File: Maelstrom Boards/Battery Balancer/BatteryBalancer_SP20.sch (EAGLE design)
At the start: 83 parts, among them IC3 REG1117, P1 39-30-14, P2 39-30-16, Q1 SPB80P06P, Q10 MOSFET-NCH-AO3404A, Q11 MOSFET-NCH-AO3404A, Q19 FDD4141TO252, Q2 SPB80P06P, Q22 FDD4141TO252, Q3 NMOSFET-D2PAK-7, Q4 310mA/60V/1.6Ω, Q5 NMOSFET-D2PAK-7, Q6 FDD4141TO252, Q7 MOSFET-NCH-AO3404A, Q8 MOSFET-NCH-AO3404A, Q9 MOSFET-NCH-AO3404A

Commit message: Changed Top Connector Position
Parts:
- removed P1: 39-30-14, con-molex-mini-fit:39-30-14
- added U$4: 14PIN-VERT, Vertical_Connectors:14PIN-VERT
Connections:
- net GND: now also U$4.1-, U$4.2-, U$4.3-, U$4.4-, U$4.5-, U$4.6-, U$4.7-; no longer P1.10, P1.11, P1.12, P1.13, P1.14, P1.8, P1.9
- net MOTOR_POWER: now also U$4.1+, U$4.2+, U$4.3+, U$4.4+, U$4.5+, U$4.6+, U$4.7+; no longer P1.1, P1.2, P1.3, P1.4, P1.5, P1.6, P1.7
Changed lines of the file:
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@@
 <part name="+3V1" library="supply1" library_urn="urn:adsk.eagle:library:371" deviceset="+3V3" device=""/>
 <part name="FRAME1" library="frames" library_urn="urn:adsk.eagle:library:229" deviceset="A3L-LOC" device="" value="a"/>
-<part name="GND4" library="supply1" library_urn="urn:adsk.eagle:library:371" deviceset="GND" device=""/>
 <part name="GND16" library="supply1" library_urn="urn:adsk.eagle:library:371" deviceset="GND" device=""/>
 <part name="P2" library="con-molex-mini-fit" deviceset="39-30-?16?" device=""/>
@@
 <part name="+3V9" library="supply1" library_urn="urn:adsk.eagle:library:371" deviceset="+3V3" device=""/>
 <part name="GND3" library="supply1" library_urn="urn:adsk.eagle:library:371" deviceset="GND" device=""/>
-<part name="P1" library="con-molex-mini-fit" deviceset="39-30-?14?" device=""/>
 <part name="GND15" library="supply1" library_urn="urn:adsk.eagle:library:371" deviceset="GND" device=""/>
 <part name="GND24" library="supply1" library_urn="urn:adsk.eagle:library:371" deviceset="GND" device=""/>
 <part name="GND25" library="supply1" library_urn="urn:adsk.eagle:library:371" deviceset="GND" device=""/>
+<part name="GND4" library="supply1" library_urn="urn:adsk.eagle:library:371" deviceset="GND" device=""/>
+<part name="U$4" library="Vertical_Connectors" deviceset="14PIN-VERT" device=""/>
 </parts>
 <sheets>
@@
 <attribute name="SHEET" x="357.680259375" y="4.9784" size="2.54" layer="94"/>
 </instance>
-<instance part="GND4" gate="1" x="353.06" y="96.52" smashed="yes">
-<attribute name="VALUE" x="350.52" y="93.98" size="1.778" layer="96"/>
-</instance>
 <instance part="GND16" gate="1" x="208.28" y="170.18" smashed="yes">
 <attribute name="VALUE" x="205.74" y="167.64" size="1.778" layer="96"/>
@@
 <attribute name="VALUE" x="88.9" y="182.88" size="1.778" layer="96"/>
 </instance>
-<instance part="P1" gate="G$1" x="335.28" y="101.6" smashed="yes">
-<attribute name="NAME" x="331.47" y="112.395" size="1.778" layer="95"/>
-<attribute name="VALUE" x="331.47" y="88.9" size="1.778" layer="95"/>
+<instance part="GND4" gate="1" x="327.66" y="104.14" smashed="yes">
+<attribute name="VALUE" x="325.12" y="101.6" size="1.778" layer="96"/>
 </instance>
+<instance part="U$4" gate="G$1" x="297.18" y="91.44" smashed="yes"/>
 </instances>
 <busses>
@@
 </segment>
 <segment>
+<pinref part="U$4" gate="G$1" pin="7-"/>
+<wire x1="312.42" y1="124.46" x2="320.04" y2="124.46" width="0.1524" layer="91"/>
+<wire x1="320.04" y1="124.46" x2="320.04" y2="119.38" width="0.1524" layer="91"/>
+<pinref part="U$4" gate="G$1" pin="1-"/>
+<wire x1="320.04" y1="119.38" x2="320.04" y2="114.3" width="0.1524" layer="91"/>
+<wire x1="320.04" y1="114.3" x2="320.04" y2="109.22" width="0.1524" layer="91"/>
+<wire x1="320.04" y1="109.22" x2="320.04" y2="104.14" width="0.1524" layer="91"/>
+<wire x1="320.04" y1="104.14" x2="320.04" y2="99.06" width="0.1524" layer="91"/>
+<wire x1="320.04" y1="99.06" x2="320.04" y2="93.98" width="0.1524" layer="91"/>
+<wire x1="320.04" y1="93.98" x2="312.42" y2="93.98" width="0.1524" layer="91"/>
+<pinref part="U$4" gate="G$1" pin="2-"/>
+<wire x1="312.42" y1="99.06" x2="320.04" y2="99.06" width="0.1524" layer="91"/>
+<junction x="320.04" y="99.06"/>
+<pinref part="U$4" gate="G$1" pin="3-"/>
+<wire x1="312.42" y1="104.14" x2="320.04" y2="104.14" width="0.1524" layer="91"/>
+<junction x="320.04" y="104.14"/>
+<pinref part="U$4" gate="G$1" pin="4-"/>
+<wire x1="312.42" y1="109.22" x2="320.04" y2="109.22" width="0.1524" layer="91"/>
+<junction x="320.04" y="109.22"/>
+<pinref part="U$4" gate="G$1" pin="5-"/>
+<wire x1="312.42" y1="114.3" x2="320.04" y2="114.3" width="0.1524" layer="91"/>
+<junction x="320.04" y="114.3"/>
+<pinref part="U$4" gate="G$1" pin="6-"/>
+<wire x1="312.42" y1="119.38" x2="320.04" y2="119.38" width="0.1524" layer="91"/>
+<junction x="320.04" y="119.38"/>
+<wire x1="320.04" y1="109.22" x2="327.66" y2="109.22" width="0.1524" layer="91"/>
 <pinref part="GND4" gate="1" pin="GND"/>
-<wire x1="353.06" y1="101.6" x2="353.06" y2="99.06" width="0.1524" layer="91"/>
-<pinref part="P1" gate="G$1" pin="10"/>
-<wire x1="342.9" y1="99.06" x2="345.44" y2="99.06" width="0.1524" layer="91"/>
-<wire x1="345.44" y1="99.06" x2="345.44" y2="101.6" width="0.1524" layer="91"/>
-<pinref part="P1" gate="G$1" pin="8"/>
-<wire x1="342.9" y1="101.6" x2="345.44" y2="101.6" width="0.1524" layer="91"/>
-<junction x="345.44" y="101.6"/>
-<pinref part="P1" gate="G$1" pin="12"/>
-<wire x1="342.9" y1="96.52" x2="345.44" y2="96.52" width="0.1524" layer="91"/>
-<wire x1="345.44" y1="96.52" x2="345.44" y2="99.06" width="0.1524" layer="91"/>
-<junction x="345.44" y="99.06"/>
-<pinref part="P1" gate="G$1" pin="14"/>
-<wire x1="342.9" y1="93.98" x2="345.44" y2="93.98" width="0.1524" layer="91"/>
-<wire x1="345.44" y1="93.98" x2="345.44" y2="96.52" width="0.1524" layer="91"/>
-<junction x="345.44" y="96.52"/>
-<wire x1="353.06" y1="101.6" x2="345.44" y2="101.6" width="0.1524" layer="91"/>
-<pinref part="P1" gate="G$1" pin="13"/>
-<pinref part="P1" gate="G$1" pin="11"/>
-<pinref part="P1" gate="G$1" pin="9"/>
-<wire x1="327.66" y1="99.06" x2="325.12" y2="99.06" width="0.1524" layer="91"/>
-<wire x1="325.12" y1="99.06" x2="325.12" y2="96.52" width="0.1524" layer="91"/>
-<wire x1="325.12" y1="96.52" x2="327.66" y2="96.52" width="0.1524" layer="91"/>
-<junction x="325.12" y="96.52"/>
-<wire x1="325.12" y1="96.52" x2="325.12" y2="93.98" width="0.1524" layer="91"/>
-<wire x1="325.12" y1="93.98" x2="327.66" y2="93.98" width="0.1524" layer="91"/>
-<wire x1="325.12" y1="93.98" x2="325.12" y2="86.36" width="0.1524" layer="91"/>
-<junction x="325.12" y="93.98"/>
-<wire x1="325.12" y1="86.36" x2="345.44" y2="86.36" width="0.1524" layer="91"/>
-<wire x1="345.44" y1="86.36" x2="345.44" y2="93.98" width="0.1524" layer="91"/>
-<junction x="345.44" y="93.98"/>
+<wire x1="327.66" y1="109.22" x2="327.66" y2="106.68" width="0.1524" layer="91"/>
 </segment>
 </net>
@@
 <junction x="198.12" y="228.6"/>
 <label x="205.74" y="233.68" size="1.778" layer="95" xref="yes"/>
-</segment>
-</net>
-<net name="MOTOR_POWER" class="0">
-<segment>
-<wire x1="325.12" y1="101.6" x2="312.42" y2="101.6" width="0.1524" layer="91"/>
-<label x="312.42" y="101.6" size="1.778" layer="95" rot="R180" xref="yes"/>
-<pinref part="P1" gate="G$1" pin="1"/>
-<wire x1="327.66" y1="109.22" x2="325.12" y2="109.22" width="0.1524" layer="91"/>
-<wire x1="325.12" y1="109.22" x2="325.12" y2="106.68" width="0.1524" layer="91"/>
-<pinref part="P1" gate="G$1" pin="3"/>
-<wire x1="325.12" y1="106.68" x2="327.66" y2="106.68" width="0.1524" layer="91"/>
-<wire x1="325.12" y1="106.68" x2="325.12" y2="104.14" width="0.1524" layer="91"/>
-<junction x="325.12" y="106.68"/>
-<pinref part="P1" gate="G$1" pin="5"/>
-<wire x1="325.12" y1="104.14" x2="327.66" y2="104.14" width="0.1524" layer="91"/>
-<wire x1="325.12" y1="104.14" x2="325.12" y2="101.6" width="0.1524" layer="91"/>
-<junction x="325.12" y="104.14"/>
-<pinref part="P1" gate="G$1" pin="7"/>
-<wire x1="325.12" y1="101.6" x2="327.66" y2="101.6" width="0.1524" layer="91"/>
-<junction x="325.12" y="101.6"/>
-<wire x1="325.12" y1="109.22" x2="325.12" y2="116.84" width="0.1524" layer="91"/>
-<junction x="325.12" y="109.22"/>
-<wire x1="325.12" y1="116.84" x2="345.44" y2="116.84" width="0.1524" layer="91"/>
-<pinref part="P1" gate="G$1" pin="2"/>
-<wire x1="345.44" y1="109.22" x2="342.9" y2="109.22" width="0.1524" layer="91"/>
-<pinref part="P1" gate="G$1" pin="4"/>
-<wire x1="342.9" y1="106.68" x2="345.44" y2="106.68" width="0.1524" layer="91"/>
-<junction x="345.44" y="106.68"/>
-<wire x1="345.44" y1="106.68" x2="345.44" y2="109.22" width="0.1524" layer="91"/>
-<wire x1="345.44" y1="104.14" x2="345.44" y2="106.68" width="0.1524" layer="91"/>
-<pinref part="P1" gate="G$1" pin="6"/>
-<wire x1="342.9" y1="104.14" x2="345.44" y2="104.14" width="0.1524" layer="91"/>
-<wire x1="345.44" y1="116.84" x2="345.44" y2="109.22" width="0.1524" layer="91"/>
-<junction x="345.44" y="109.22"/>
 </segment>
 </net>
@@
 </segment>
 </net>
+<net name="MOTOR_POWER" class="0">
+<segment>
+<pinref part="U$4" gate="G$1" pin="7+"/>
+<wire x1="292.1" y1="124.46" x2="284.48" y2="124.46" width="0.1524" layer="91"/>
+<pinref part="U$4" gate="G$1" pin="1+"/>
+<wire x1="284.48" y1="124.46" x2="284.48" y2="119.38" width="0.1524" layer="91"/>
+<wire x1="284.48" y1="119.38" x2="284.48" y2="114.3" width="0.1524" layer="91"/>
+<wire x1="284.48" y1="114.3" x2="284.48" y2="109.22" width="0.1524" layer="91"/>
+<wire x1="284.48" y1="109.22" x2="284.48" y2="104.14" width="0.1524" layer="91"/>
+<wire x1="284.48" y1="104.14" x2="284.48" y2="99.06" width="0.1524" layer="91"/>
+<wire x1="284.48" y1="99.06" x2="284.48" y2="93.98" width="0.1524" layer="91"/>
+<wire x1="284.48" y1="93.98" x2="292.1" y2="93.98" width="0.1524" layer="91"/>
+<pinref part="U$4" gate="G$1" pin="2+"/>
+<wire x1="292.1" y1="99.06" x2="284.48" y2="99.06" width="0.1524" layer="91"/>
+<junction x="284.48" y="99.06"/>
+<pinref part="U$4" gate="G$1" pin="3+"/>
+<wire x1="292.1" y1="104.14" x2="284.48" y2="104.14" width="0.1524" layer="91"/>
+<junction x="284.48" y="104.14"/>
+<pinref part="U$4" gate="G$1" pin="4+"/>
+<wire x1="292.1" y1="109.22" x2="284.48" y2="109.22" width="0.1524" layer="91"/>
+<junction x="284.48" y="109.22"/>
+<pinref part="U$4" gate="G$1" pin="5+"/>
+<wire x1="292.1" y1="114.3" x2="284.48" y2="114.3" width="0.1524" layer="91"/>
+<junction x="284.48" y="114.3"/>
+<pinref part="U$4" gate="G$1" pin="6+"/>
+<wire x1="292.1" y1="119.38" x2="284.48" y2="119.38" width="0.1524" layer="91"/>
+<junction x="284.48" y="119.38"/>
+<wire x1="284.48" y1="109.22" x2="274.32" y2="109.22" width="0.1524" layer="91"/>
+<label x="274.32" y="109.22" size="1.778" layer="95" rot="R180" xref="yes"/>
+</segment>
+</net>

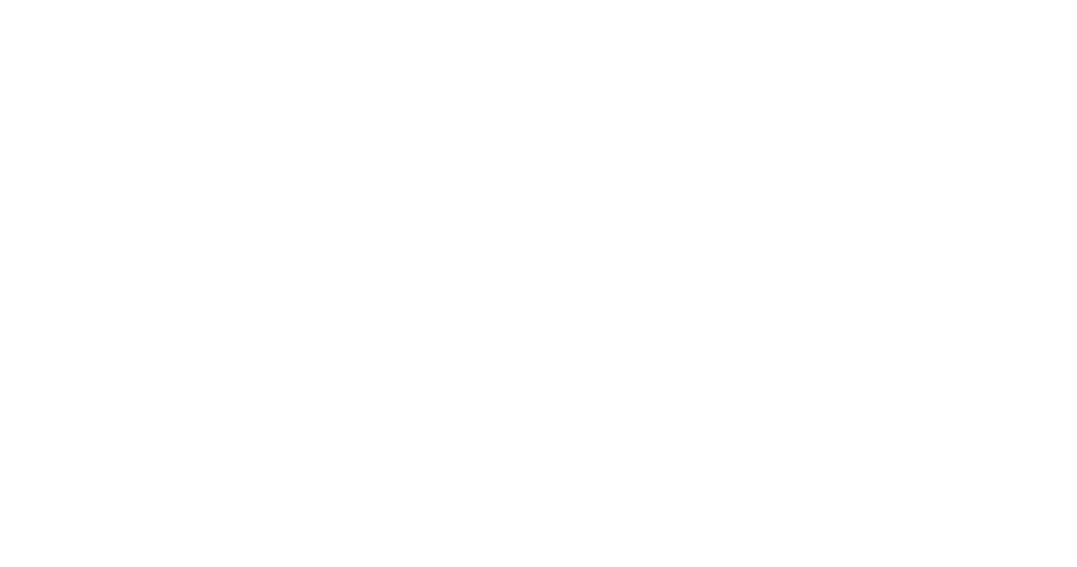
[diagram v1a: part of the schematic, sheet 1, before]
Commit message: Added connector to BB
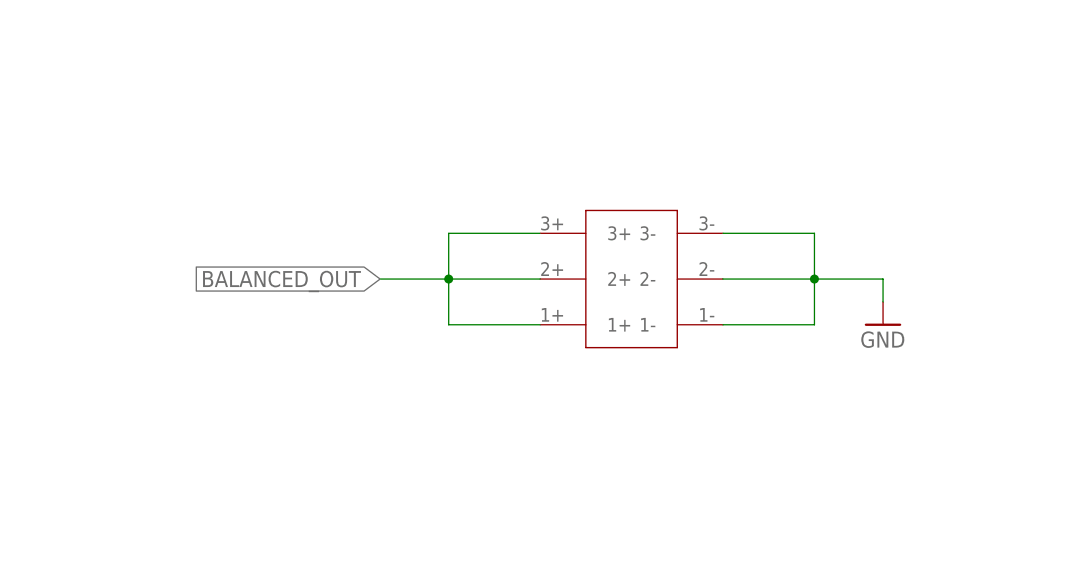
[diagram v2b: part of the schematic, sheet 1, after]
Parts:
- added U$13: 6PIN-VERT, Vertical_Connectors:6PIN-VERT
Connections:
- removed net V+: L1.1, L3.1, R20.1, R22.1, R5.1
- net BALANCED_OUT: now also L1.1, L3.1, R20.1, R22.1, R5.1, U$13.1+, U$13.2+, U$13.3+
- net GND: now also U$13.1-, U$13.2-, U$13.3-
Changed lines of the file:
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@@
 <part name="P+2" library="supply1" library_urn="urn:adsk.eagle:library:371" deviceset="+12V" device=""/>
 <part name="Q11" library="SparkFun-DiscreteSemi" deviceset="MOSFET-NCH" device="-AO3404A" value=""/>
-<part name="P+3" library="supply1" library_urn="urn:adsk.eagle:library:371" deviceset="V+" device=""/>
+<part name="BALANCED_OUT" library="supply1" library_urn="urn:adsk.eagle:library:371" deviceset="V+" device=""/>
 <part name="P+4" library="supply1" library_urn="urn:adsk.eagle:library:371" deviceset="V+" device=""/>
 <part name="P+8" library="supply1" library_urn="urn:adsk.eagle:library:371" deviceset="V+" device=""/>
@@
 <part name="GND4" library="supply1" library_urn="urn:adsk.eagle:library:371" deviceset="GND" device=""/>
 <part name="U$4" library="Vertical_Connectors" deviceset="14PIN-VERT" device=""/>
+<part name="U$13" library="Vertical_Connectors" deviceset="6PIN-VERT" device=""/>
+<part name="GND26" library="supply1" library_urn="urn:adsk.eagle:library:371" deviceset="GND" device=""/>
 </parts>
 <sheets>
@@
 </instance>
 <instance part="U$4" gate="G$1" x="297.18" y="91.44" smashed="yes"/>
+<instance part="U$13" gate="G$1" x="307.34" y="187.96" smashed="yes"/>
+<instance part="GND26" gate="1" x="340.36" y="190.5" smashed="yes">
+<attribute name="VALUE" x="337.82" y="187.96" size="1.778" layer="96"/>
+</instance>
 </instances>
 <busses>
@@
 <wire x1="327.66" y1="109.22" x2="327.66" y2="106.68" width="0.1524" layer="91"/>
 </segment>
+<segment>
+<pinref part="GND26" gate="1" pin="GND"/>
+<wire x1="340.36" y1="193.04" x2="340.36" y2="195.58" width="0.1524" layer="91"/>
+<wire x1="340.36" y1="195.58" x2="332.74" y2="195.58" width="0.1524" layer="91"/>
+<pinref part="U$13" gate="G$1" pin="3-"/>
+<wire x1="322.58" y1="200.66" x2="332.74" y2="200.66" width="0.1524" layer="91"/>
+<wire x1="332.74" y1="200.66" x2="332.74" y2="195.58" width="0.1524" layer="91"/>
+<pinref part="U$13" gate="G$1" pin="1-"/>
+<wire x1="332.74" y1="195.58" x2="332.74" y2="190.5" width="0.1524" layer="91"/>
+<wire x1="332.74" y1="190.5" x2="322.58" y2="190.5" width="0.1524" layer="91"/>
+<pinref part="U$13" gate="G$1" pin="2-"/>
+<wire x1="322.58" y1="195.58" x2="332.74" y2="195.58" width="0.1524" layer="91"/>
+<junction x="332.74" y="195.58"/>
+</segment>
 </net>
 <net name="STBD_BATTERY" class="0">
@@
 </segment>
 </net>
+<net name="BALANCED_OUT" class="0">
+<segment>
+<pinref part="U$13" gate="G$1" pin="1+"/>
+<wire x1="302.26" y1="190.5" x2="292.1" y2="190.5" width="0.1524" layer="91"/>
+<wire x1="292.1" y1="190.5" x2="292.1" y2="195.58" width="0.1524" layer="91"/>
+<pinref part="U$13" gate="G$1" pin="3+"/>
+<wire x1="292.1" y1="195.58" x2="292.1" y2="200.66" width="0.1524" layer="91"/>
+<wire x1="292.1" y1="200.66" x2="302.26" y2="200.66" width="0.1524" layer="91"/>
+<pinref part="U$13" gate="G$1" pin="2+"/>
+<wire x1="302.26" y1="195.58" x2="292.1" y2="195.58" width="0.1524" layer="91"/>
+<junction x="292.1" y="195.58"/>
+<wire x1="292.1" y1="195.58" x2="284.48" y2="195.58" width="0.1524" layer="91"/>
+<label x="284.48" y="195.58" size="1.778" layer="95" rot="R180" xref="yes"/>
+</segment>
+</net>
 </nets>
 </sheet>
@@
 <attribute name="VALUE" x="227.33" y="159.258" size="1.778" layer="96"/>
 </instance>
-<instance part="P+3" gate="1" x="233.68" y="200.66" smashed="yes" rot="R270">
-<attribute name="VALUE" x="231.14" y="203.2" size="1.778" layer="96"/>
-</instance>
+<instance part="BALANCED_OUT" gate="1" x="233.68" y="200.66" smashed="yes" rot="R270"/>
 </instances>
 <busses>
@@
 </segment>
 </net>
-<net name="BALANCED_OUT" class="0">
-<segment>
-<pinref part="U$2" gate="G$1" pin="OUT"/>
-<wire x1="193.04" y1="218.44" x2="193.04" y2="215.9" width="0.1524" layer="91"/>
-<wire x1="193.04" y1="218.44" x2="210.82" y2="218.44" width="0.1524" layer="91"/>
-<wire x1="210.82" y1="218.44" x2="210.82" y2="208.28" width="0.1524" layer="91"/>
-<junction x="193.04" y="218.44"/>
-<pinref part="U$2" gate="G$1" pin="VS"/>
-<wire x1="210.82" y1="208.28" x2="210.82" y2="198.12" width="0.1524" layer="91"/>
-<wire x1="210.82" y1="198.12" x2="203.2" y2="198.12" width="0.1524" layer="91"/>
-<wire x1="210.82" y1="208.28" x2="220.98" y2="208.28" width="0.1524" layer="91"/>
-<junction x="210.82" y="208.28"/>
-<wire x1="208.28" y1="109.22" x2="220.98" y2="109.22" width="0.1524" layer="91"/>
-<pinref part="U$3" gate="G$1" pin="OUT"/>
-<wire x1="193.04" y1="129.54" x2="193.04" y2="127" width="0.1524" layer="91"/>
-<junction x="193.04" y="129.54"/>
-<wire x1="193.04" y1="129.54" x2="208.28" y2="129.54" width="0.1524" layer="91"/>
-<wire x1="208.28" y1="129.54" x2="208.28" y2="109.22" width="0.1524" layer="91"/>
-<junction x="208.28" y="109.22"/>
-<pinref part="U$3" gate="G$1" pin="VS"/>
-<wire x1="203.2" y1="109.22" x2="208.28" y2="109.22" width="0.1524" layer="91"/>
-<wire x1="220.98" y1="109.22" x2="220.98" y2="162.56" width="0.1524" layer="91"/>
-<wire x1="220.98" y1="162.56" x2="220.98" y2="170.18" width="0.1524" layer="91"/>
-<wire x1="220.98" y1="170.18" x2="220.98" y2="208.28" width="0.1524" layer="91"/>
-<wire x1="226.06" y1="170.18" x2="220.98" y2="170.18" width="0.1524" layer="91"/>
-<junction x="220.98" y="170.18"/>
-<pinref part="R12" gate="G$1" pin="1"/>
-<pinref part="Q3" gate="G$1" pin="D"/>
-<wire x1="190.5" y1="233.68" x2="193.04" y2="233.68" width="0.1524" layer="91"/>
-<wire x1="193.04" y1="233.68" x2="193.04" y2="218.44" width="0.1524" layer="91"/>
-<pinref part="Q5" gate="G$1" pin="D"/>
-<wire x1="190.5" y1="144.78" x2="193.04" y2="144.78" width="0.1524" layer="91"/>
-<wire x1="193.04" y1="144.78" x2="193.04" y2="129.54" width="0.1524" layer="91"/>
-<pinref part="R19" gate="G$1" pin="1"/>
-<wire x1="226.06" y1="162.56" x2="220.98" y2="162.56" width="0.1524" layer="91"/>
-<junction x="220.98" y="162.56"/>
-</segment>
-</net>
 <net name="N$11" class="0">
 <segment>
@@
 </segment>
 </net>
-<net name="V+" class="0">
+<net name="BALANCED_OUT" class="0">
 <segment>
-<pinref part="P+3" gate="1" pin="V+"/>
+<pinref part="U$2" gate="G$1" pin="OUT"/>
+<wire x1="193.04" y1="218.44" x2="193.04" y2="215.9" width="0.1524" layer="91"/>
+<wire x1="193.04" y1="218.44" x2="210.82" y2="218.44" width="0.1524" layer="91"/>
+<wire x1="210.82" y1="218.44" x2="210.82" y2="208.28" width="0.1524" layer="91"/>
+<junction x="193.04" y="218.44"/>
+<pinref part="U$2" gate="G$1" pin="VS"/>
+<wire x1="210.82" y1="208.28" x2="210.82" y2="198.12" width="0.1524" layer="91"/>
+<wire x1="210.82" y1="198.12" x2="203.2" y2="198.12" width="0.1524" layer="91"/>
+<wire x1="210.82" y1="208.28" x2="220.98" y2="208.28" width="0.1524" layer="91"/>
+<junction x="210.82" y="208.28"/>
+<wire x1="208.28" y1="109.22" x2="220.98" y2="109.22" width="0.1524" layer="91"/>
+<pinref part="U$3" gate="G$1" pin="OUT"/>
+<wire x1="193.04" y1="129.54" x2="193.04" y2="127" width="0.1524" layer="91"/>
+<junction x="193.04" y="129.54"/>
+<wire x1="193.04" y1="129.54" x2="208.28" y2="129.54" width="0.1524" layer="91"/>
+<wire x1="208.28" y1="129.54" x2="208.28" y2="109.22" width="0.1524" layer="91"/>
+<junction x="208.28" y="109.22"/>
+<pinref part="U$3" gate="G$1" pin="VS"/>
+<wire x1="203.2" y1="109.22" x2="208.28" y2="109.22" width="0.1524" layer="91"/>
+<wire x1="220.98" y1="109.22" x2="220.98" y2="162.56" width="0.1524" layer="91"/>
+<wire x1="220.98" y1="162.56" x2="220.98" y2="170.18" width="0.1524" layer="91"/>
+<wire x1="220.98" y1="170.18" x2="220.98" y2="200.66" width="0.1524" layer="91"/>
+<wire x1="220.98" y1="200.66" x2="220.98" y2="208.28" width="0.1524" layer="91"/>
+<wire x1="226.06" y1="170.18" x2="220.98" y2="170.18" width="0.1524" layer="91"/>
+<junction x="220.98" y="170.18"/>
+<pinref part="R12" gate="G$1" pin="1"/>
+<pinref part="Q3" gate="G$1" pin="D"/>
+<wire x1="190.5" y1="233.68" x2="193.04" y2="233.68" width="0.1524" layer="91"/>
+<wire x1="193.04" y1="233.68" x2="193.04" y2="218.44" width="0.1524" layer="91"/>
+<pinref part="Q5" gate="G$1" pin="D"/>
+<wire x1="190.5" y1="144.78" x2="193.04" y2="144.78" width="0.1524" layer="91"/>
+<wire x1="193.04" y1="144.78" x2="193.04" y2="129.54" width="0.1524" layer="91"/>
+<pinref part="R19" gate="G$1" pin="1"/>
+<wire x1="226.06" y1="162.56" x2="220.98" y2="162.56" width="0.1524" layer="91"/>
+<junction x="220.98" y="162.56"/>
+<pinref part="BALANCED_OUT" gate="1" pin="V+"/>
 <wire x1="231.14" y1="200.66" x2="220.98" y2="200.66" width="0.1524" layer="91"/>
+<junction x="220.98" y="200.66"/>
+<label x="231.14" y="203.2" size="1.778" layer="95"/>
 </segment>
 </net>
@@
 </segment>
 </net>
-<net name="V+" class="0">
+<net name="BALANCED_OUT" class="0">
 <segment>
 <pinref part="P+8" gate="1" pin="V+"/>
@@
 </segment>
 </net>
-<net name="V+" class="0">
+<net name="BALANCED_OUT" class="0">
 <segment>
 <pinref part="R20" gate="G$1" pin="1"/>
